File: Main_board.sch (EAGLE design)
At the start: 65 parts, among them U2 TPS61200, U3 MAX1704X, U4 USD-SOCKETNEW, U5 TPS61200, X1 USB-MICROB, Y1 16MHz KX-7

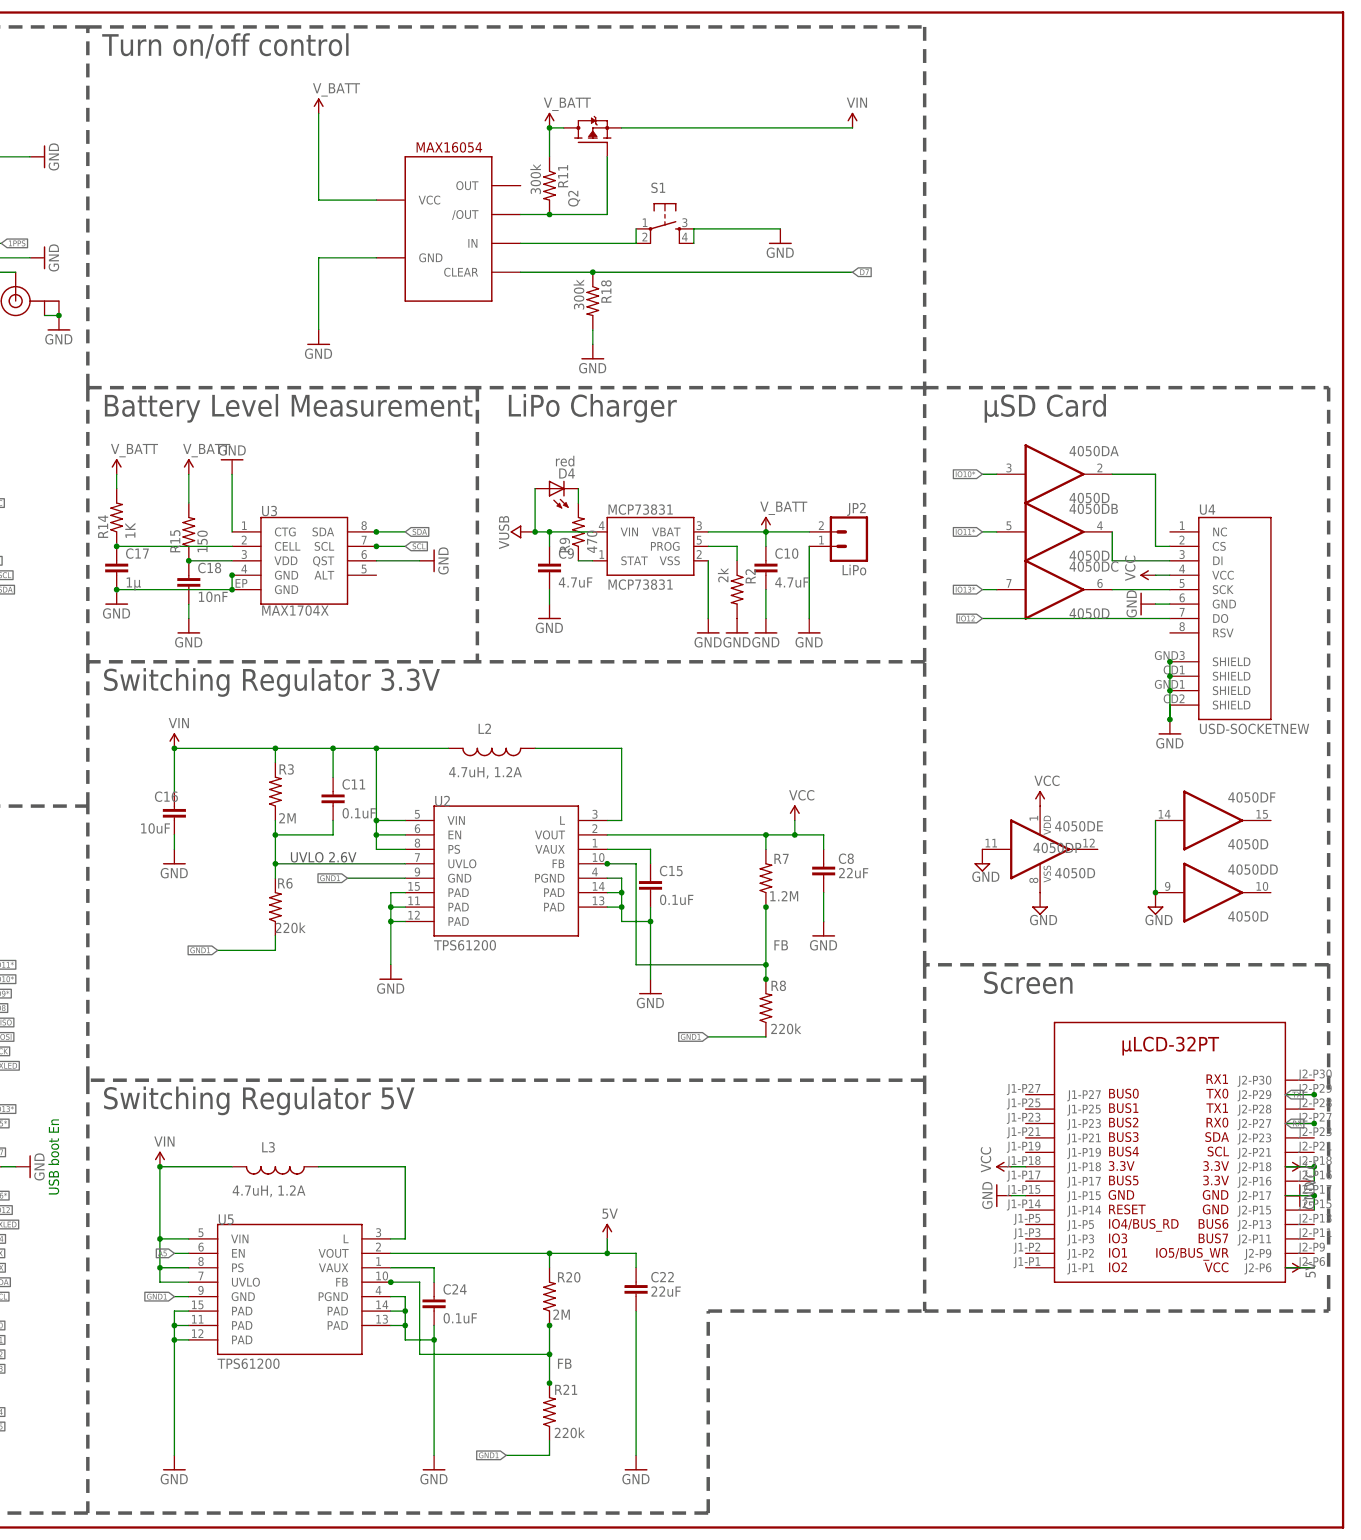
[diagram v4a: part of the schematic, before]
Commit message: 3V3 boost converter replacement
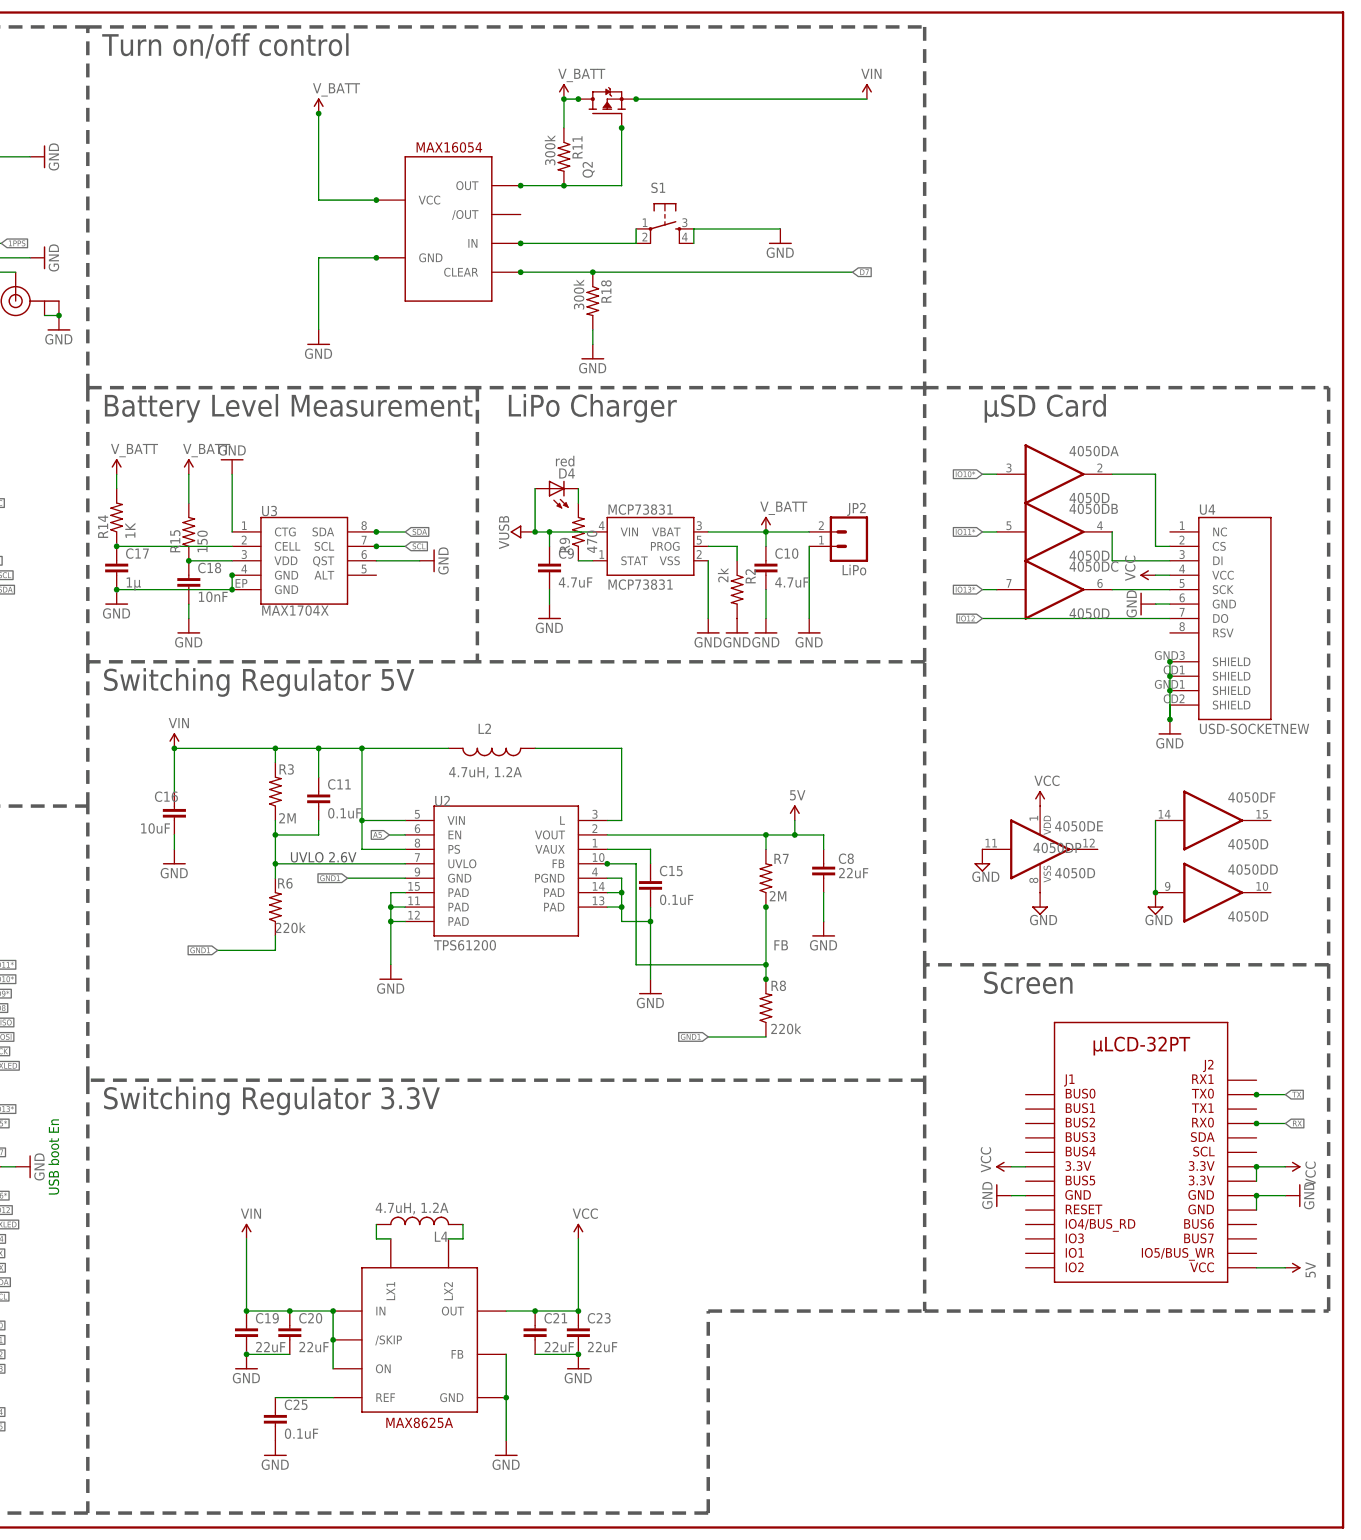
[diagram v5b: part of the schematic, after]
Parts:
- removed C22: 22uF, SparkFun:CAP0805
- removed C24: 0.1uF, SparkFun:CAP0805
- removed L3: 4.7uH, 1.2A, SparkFun:INDUCTOR.
- removed R20: 2M, SparkFun:RESISTOR0805-RES
- removed R21: 220k, SparkFun:RESISTOR0805-RES
- removed U5: TPS61200, SparkFun:TPS61200
- added C19, C20, C21, C23: 22uF, SparkFun:CAP0805
- added C25: 0.1uF, SparkFun:CAP0805
- added L4: 4.7uH, 1.2A, rcl:L-US
- added MAX16054: MAX16054, maxim:MAX16054
- L2: device SparkFun:INDUCTOR. -> rcl:L-US
- R7: value 1.2M -> 2M
- U$9: value MAX16054 -> MAX8625A; device maxim:MAX16054 -> maxim:MAX8625A
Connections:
- removed net N$16: L3.1, U5.L
- removed net N$17: C24.1, U5.VAUX
- new net N$22: C25.1, U$9.REF
- new net N$23: L4.1, U$9.LX1
- new net N$24: L4.2, U$9.LX2
- net 5V: now also C8.1, R7.2, U2.VOUT; no longer C22.1, R20.2, U5.VOUT
- net A5: now also U2.EN; no longer U5.EN
- net D7: now also MAX16054.CLEAR; no longer U$9.CLEAR
- net FB: no longer R20.1, R21.2, U5.FB
- net GND: now also C19.2, C20.2, C21.2, C23.2, C25.2, MAX16054.GND, U$9.FB; no longer C22.2, C24.2, U5.PAD@1, U5.PAD@2, U5.PAD@3, U5.PAD@4, U5.PAD@5, U5.PGND
- net GND1: no longer R21.1, U5.GND
- net N$15: now also MAX16054.IN; no longer U$9.IN
- net N$19: now also MAX16054.OUT; no longer U$9./OUT
- net VCC: now also C21.1, C23.1, U$9.OUT; no longer C8.1, R7.2, U2.VOUT
- net VIN: now also C19.1, C20.1, U$9./SKIP, U$9.IN, U$9.ON; no longer L3.2, U2.EN, U5.PS, U5.UVLO, U5.VIN
- net V_BATT: now also MAX16054.VCC
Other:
- moved on the sheet: C11, Q2, R11

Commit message: Board routing + cleaning
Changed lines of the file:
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@@
 <wire x1="287.02" y1="226.06" x2="287.02" y2="228.6" width="0.1524" layer="91"/>
 <pinref part="GND38" gate="1" pin="GND"/>
+<junction x="287.02" y="228.6"/>
 </segment>
 <segment>
@@
 <wire x1="276.86" y1="226.06" x2="256.54" y2="226.06" width="0.1524" layer="91"/>
 <junction x="256.54" y="226.06"/>
+<junction x="276.86" y="226.06"/>
 </segment>
 </net>
@@
 </sheet>
 </sheets>
+<errors>
+</errors>
 </schematic>
 </drawing>

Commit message: Update to board
Alignement to grid, and thickness of traces adjuted
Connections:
- net N$19 renamed V_CTRL
- net VCC: no longer U$2.J1-P18, U$2.J2-P16, U$2.J2-P18
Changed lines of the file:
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@@
 <part name="GND44" library="SparkFun" deviceset="GND" device=""/>
 <part name="GND45" library="SparkFun" deviceset="GND" device=""/>
-<part name="P+4" library="SparkFun" deviceset="VCC" device=""/>
-<part name="P+5" library="SparkFun" deviceset="VCC" device=""/>
 <part name="FRAME1" library="frames" deviceset="TABL_L" device=""/>
 <part name="U$6" library="SparkFun-Breakouts" deviceset="HMC5883" device=""/>
@@
 <instance part="GND44" gate="1" x="393.7" y="58.42" rot="R90"/>
 <instance part="GND45" gate="1" x="340.36" y="58.42" rot="R270"/>
-<instance part="P+4" gate="1" x="391.16" y="63.5" rot="R270"/>
-<instance part="P+5" gate="1" x="342.9" y="63.5" rot="R90"/>
 <instance part="FRAME1" gate="G$1" x="0" y="0"/>
 <instance part="FRAME1" gate="G$2" x="299.72" y="0"/>
@@
 </segment>
 <segment>
-<pinref part="U$2" gate="G$1" pin="J2-P16"/>
-<pinref part="P+4" gate="1" pin="VCC"/>
-<wire x1="391.16" y1="63.5" x2="386.08" y2="63.5" width="0.1524" layer="91"/>
-<wire x1="386.08" y1="63.5" x2="386.08" y2="60.96" width="0.1524" layer="91"/>
-<pinref part="U$2" gate="G$1" pin="J2-P18"/>
-<junction x="386.08" y="63.5"/>
-</segment>
-<segment>
-<pinref part="U$2" gate="G$1" pin="J1-P18"/>
-<pinref part="P+5" gate="1" pin="VCC"/>
-<wire x1="342.9" y1="63.5" x2="345.44" y2="63.5" width="0.1524" layer="91"/>
-</segment>
-<segment>
 <pinref part="4050D" gate="P" pin="VDD"/>
 <pinref part="P+7" gate="1" pin="VCC"/>
@@
 </segment>
 </net>
-<net name="N$19" class="0">
+<net name="V_CTRL" class="0">
 <segment>
 <pinref part="R11" gate="G$1" pin="2"/>
